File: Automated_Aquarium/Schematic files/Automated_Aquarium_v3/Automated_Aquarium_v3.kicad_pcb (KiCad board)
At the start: 2 copper layers, 50 parts, among them IC2 CH224K, IC3 LMR51420XFDDCR, J1 Screw_Terminal_01x02, J2 Screw_Terminal_01x02, K1 G3VM-61VY3_TR05_, K2 G3VM-61VY3_TR05_, P1 USB_C_Plug, Q1 BSS138P,215, Q2 PMOS, U1 ESP32-C3-MINI-1

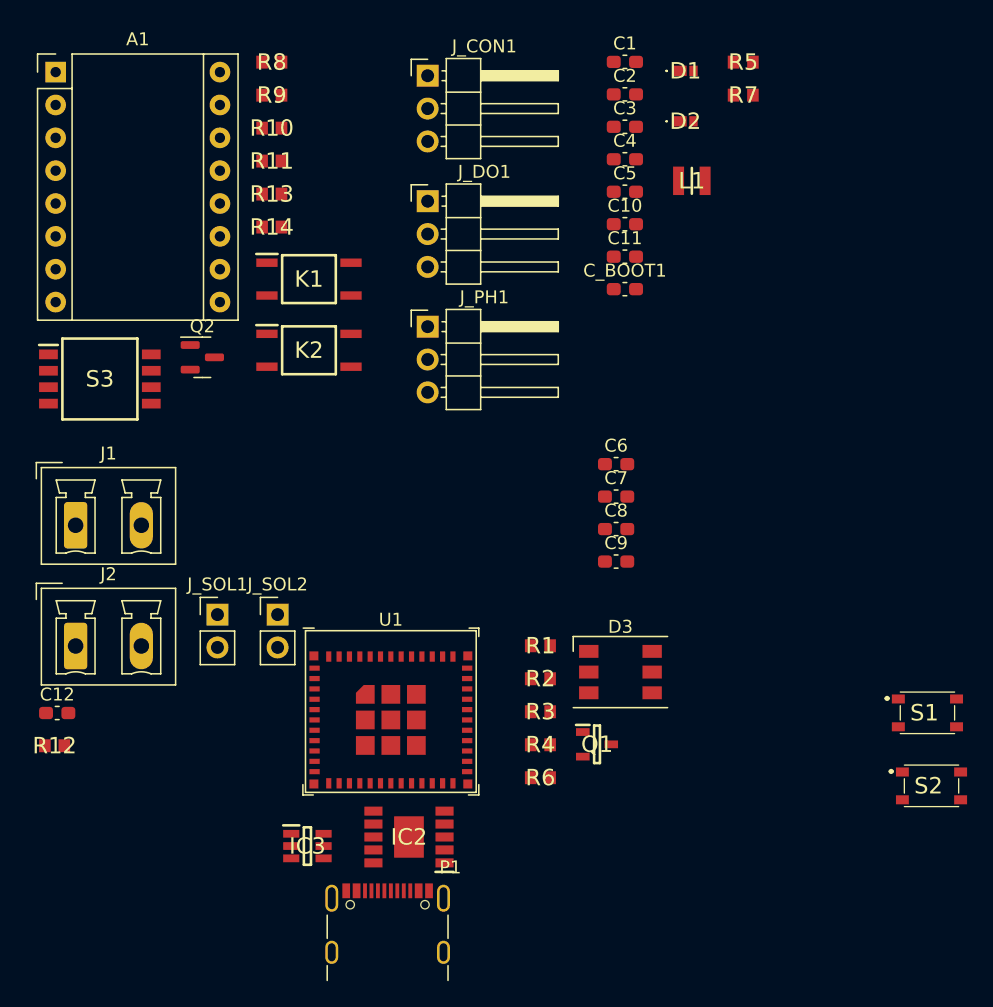
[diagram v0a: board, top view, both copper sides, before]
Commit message: finish aqua schem, add inital layout
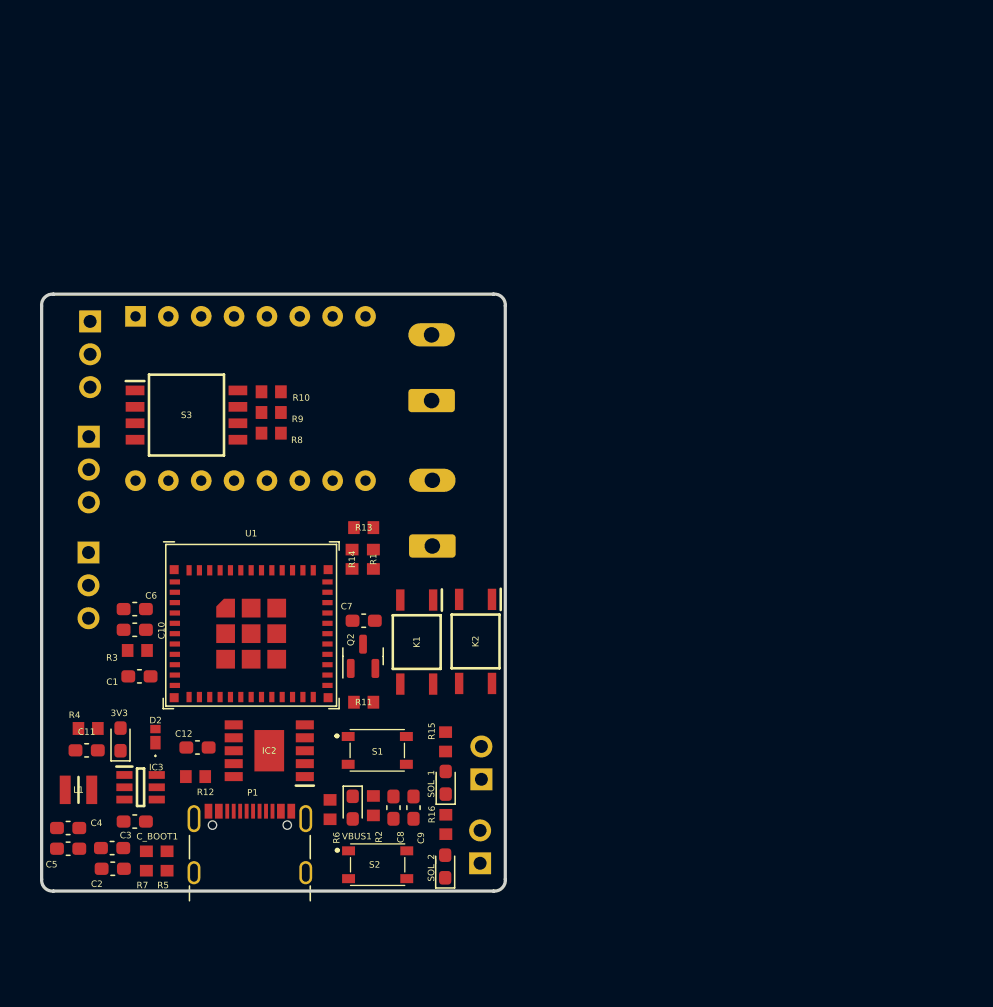
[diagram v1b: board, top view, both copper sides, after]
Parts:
- removed D1: PMEG2020EPK,315, SamacSys_Parts:PMEG2020EPK315
- removed D3: WS2813, LED_SMD:LED_WS2812_PLCC6_5.0x5.0mm_P1.6mm
- removed Q1: BSS138P,215, SamacSys_Parts:SOT95P230X110-3N
- added 3V3: LED, LED_SMD:LED_0603_1608Metric_Pad1.05x0.95mm_HandSolder, F.Cu at (150.0, 109.4)
- added R15: 15k, SamacSys_Parts:RESC1608X55N, F.Cu at (175.1, 109.5)
- added R16: 15k, SamacSys_Parts:RESC1608X55N, F.Cu at (175.2, 115.9)
- added SOL_1: LED, LED_SMD:LED_0603_1608Metric_Pad1.05x0.95mm_HandSolder, F.Cu at (175.1, 112.7)
- added SOL_2: LED, LED_SMD:LED_0603_1608Metric_Pad1.05x0.95mm_HandSolder, F.Cu at (175.1, 119.2)
- added VBUS1: LED, LED_SMD:LED_0603_1608Metric_Pad1.05x0.95mm_HandSolder, F.Cu at (167.9, 114.6)
- A1, J1, J2, J_CON1, J_DO1, J_PH1, J_SOL1, J_SOL2: moved to B.Cu
- R4: value 15k -> 1k
- moved R5 76.1 mm to (153.6, 118.8), turned to 90 degrees
- moved R7 75.1 mm to (152.0, 118.8), turned to -90 degrees
- moved C2 71.8 mm to (149.4, 119.4)
- moved C3 68.4 mm to (149.3, 117.8)
- moved C4 67.3 mm to (145.9, 116.2)
- moved L1 66.8 mm to (146.8, 113.3)
- moved C5 66.6 mm to (145.9, 117.8)
- moved D2 62.8 mm to (152.7, 109.2), turned to 90 degrees
- moved C1 60.5 mm to (151.5, 104.5)
- moved C11 56.5 mm to (147.4, 110.2)
- moved C_BOOT1 55.9 mm to (151.1, 115.7), turned to 180 degrees
- moved C10 49.2 mm to (151.1, 100.9), turned to 180 degrees
- moved S2 43.3 mm to (169.9, 119.0)
- moved S1 42.6 mm to (169.8, 110.2)
- moved R11 42.4 mm to (168.8, 106.5), turned to 180 degrees
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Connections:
- J_CON1 pad 2: unconnected-(J_CON1-Pin_2-Pad2) -> 3V3
- Q2 pad 2: /Stepper_Drivers/SOL_IN -> D5
- R13 pad 2: /Stepper_Drivers/SOL_IN -> D5
- R4 pad 1: D5 -> Net-(3V3-A)
- R6 pad 1: /ESP32/5V_DIN -> Net-(VBUS1-A)
- R6 pad 2: 5V -> VUSB
- S1 pad 2: unconnected-(S1-COM_2-Pad2) -> EN
- S1 pad 4: EN -> unconnected-(S1-NO_2-Pad4)
- S2 pad 2: unconnected-(S2-COM_2-Pad2) -> D9
- S2 pad 4: D9 -> unconnected-(S2-NO_2-Pad4)
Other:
- board outline added: 35.9 x 46.2 mm
